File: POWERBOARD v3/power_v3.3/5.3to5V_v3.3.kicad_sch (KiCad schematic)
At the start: 22 parts, among them IC1 MAX25301AATB_V+T, IC2 MCP6541T-I_OT, IC3 AP2281-1FMG-7, J3 2053380002

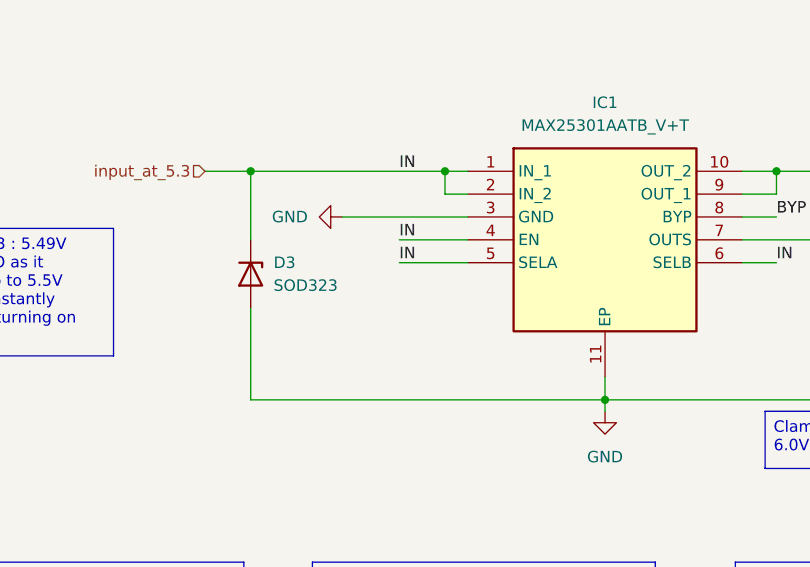
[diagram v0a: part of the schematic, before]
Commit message: Fixed D3 symbol
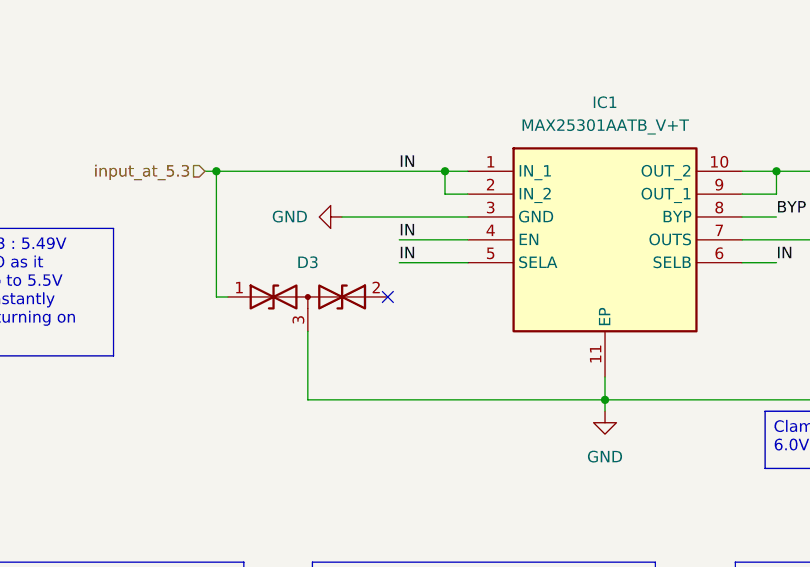
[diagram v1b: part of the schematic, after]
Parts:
- removed D3: SOD323, Package_TO_SOT_SMD:SOT-23, symbol Device:D_Zener
- added D3: SOD323, Package_TO_SOT_SMD:SOT-23, symbol Device:D_TVS_Dual_AAC
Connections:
- net GND: now also D3.3 (common)
- net input_at_5.3: now also D3.1 (A1)
- no-connect marks 2 -> 3
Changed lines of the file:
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@@
 	)
 	(junction
+		(at 95.25 57.15)
+		(diameter 0)
+		(color 0 0 0 0)
+	)
+	(junction
 		(at 205.74 57.15)
 		(diameter 0)
@@
 	)
 	(junction
-		(at 99.06 57.15)
-		(diameter 0)
-		(color 0 0 0 0)
-	)
-	(junction
 		(at 138.43 82.55)
 		(diameter 0)
@@
 	)
 	(no_connect
+		(at 114.3 71.12)
+	)
+	(no_connect
 		(at 72.39 134.62)
 	)
@@
 	(wire
 		(pts
-			(xy 228.6 116.84) (xy 240.03 116.84)
+			(xy 105.41 74.93) (xy 105.41 82.55)
 		)
 		(stroke
@@
 	(wire
 		(pts
-			(xy 153.67 67.31) (xy 157.48 67.31)
+			(xy 228.6 116.84) (xy 240.03 116.84)
 		)
 		(stroke
@@
 	(wire
 		(pts
-			(xy 62.23 168.91) (xy 62.23 175.26)
+			(xy 153.67 67.31) (xy 157.48 67.31)
 		)
 		(stroke
@@
 	(wire
 		(pts
-			(xy 231.14 82.55) (xy 236.22 82.55)
+			(xy 62.23 168.91) (xy 62.23 175.26)
 		)
 		(stroke
@@
 	(wire
 		(pts
-			(xy 99.06 72.39) (xy 99.06 82.55)
+			(xy 231.14 82.55) (xy 236.22 82.55)
 		)
 		(stroke
@@
 	(wire
 		(pts
-			(xy 99.06 82.55) (xy 138.43 82.55)
-		)
-		(stroke
-			(width 0)
-			(type default)
-		)
-	)
-	(wire
-		(pts
 			(xy 252.73 62.23) (xy 252.73 67.31)
 		)
@@
 	(wire
 		(pts
+			(xy 95.25 57.15) (xy 95.25 71.12)
+		)
+		(stroke
+			(width 0)
+			(type default)
+		)
+	)
+	(wire
+		(pts
 			(xy 179.07 152.4) (xy 189.23 152.4)
 		)
@@
 	(wire
 		(pts
+			(xy 105.41 82.55) (xy 138.43 82.55)
+		)
+		(stroke
+			(width 0)
+			(type default)
+		)
+	)
+	(wire
+		(pts
 			(xy 189.23 124.46) (xy 189.23 134.62)
 		)
@@
 	(wire
 		(pts
-			(xy 93.98 57.15) (xy 99.06 57.15)
-		)
-		(stroke
-			(width 0)
-			(type default)
-		)
-	)
-	(wire
-		(pts
 			(xy 44.45 116.84) (xy 44.45 152.4)
 		)
@@
 	(wire
 		(pts
-			(xy 99.06 57.15) (xy 99.06 64.77)
+			(xy 95.25 71.12) (xy 96.52 71.12)
 		)
 		(stroke
@@
 	(wire
 		(pts
-			(xy 99.06 57.15) (xy 120.65 57.15)
+			(xy 93.98 57.15) (xy 95.25 57.15)
 		)
 		(stroke
@@
 	(wire
 		(pts
+			(xy 95.25 57.15) (xy 120.65 57.15)
+		)
+		(stroke
+			(width 0)
+			(type default)
+		)
+	)
+	(wire
+		(pts
 			(xy 59.69 116.84) (xy 59.69 106.68)
 		)
@@
 	)
 	(symbol
-		(lib_id "Device:D_Zener")
-		(at 99.06 68.58 270)
-		(unit 1)
-		(body_style 1)
-		(exclude_from_sim no)
-		(in_bom yes)
-		(on_board yes)
-		(in_pos_files yes)
-		(dnp no)
-		(fields_autoplaced yes)
-		(property "Reference" "D3"
-			(at 101.6 67.3099 90)
-			(show_name no)
-			(do_not_autoplace no)
-			(effects
-				(font
-					(size 1.27 1.27)
-				)
-				(justify left)
-			)
-		)
-		(property "Value" "SOD323"
-			(at 101.6 69.8499 90)
-			(show_name no)
-			(do_not_autoplace no)
-			(effects
-				(font
-					(size 1.27 1.27)
-				)
-				(justify left)
-			)
-		)
-		(property "Footprint" "Package_TO_SOT_SMD:SOT-23"
-			(at 99.06 68.58 0)
-			(hide yes)
-			(show_name no)
-			(do_not_autoplace no)
-			(effects
-				(font
-					(size 1.27 1.27)
-				)
-			)
-		)
-		(property "Datasheet" "https://www.ti.com/lit/ds/symlink/esds452-q1.pdf?ts=1791562944169&ref_url=https%253A%252F%252Fwww.mouser.ch%252F"
-			(at 99.06 68.58 0)
-			(hide yes)
-			(show_name no)
-			(do_not_autoplace no)
-			(effects
-				(font
-					(size 1.27 1.27)
-				)
-			)
-		)
-		(property "Description" "Zener diode"
-			(at 99.06 68.58 0)
-			(hide yes)
-			(show_name no)
-			(do_not_autoplace no)
-			(effects
-				(font
-					(size 1.27 1.27)
-				)
-			)
-		)
-		(pin "1"
-		)
-		(pin "2"
-		)
-		(instances
-			(project "power_v3.3"
-				(path "/432bcdcf-747a-4fa0-b87b-096f44260199/9585df76-13b3-4fa5-b448-53940051778a"
-					(reference "D3")
-					(unit 1)
-				)
-			)
-		)
-	)
-	(symbol
 		(lib_id "power:GND")
 		(at 189.23 154.94 0)
@@
 					(unit 1)
 				)
+			)
+		)
+	)
+	(symbol
+		(lib_id "Device:D_TVS_Dual_AAC")
+		(at 105.41 71.12 0)
+		(unit 1)
+		(body_style 1)
+		(exclude_from_sim no)
+		(in_bom yes)
+		(on_board yes)
+		(in_pos_files yes)
+		(dnp no)
+		(fields_autoplaced yes)
+		(property "Reference" "D3"
+			(at 105.41 67.31 0)
+			(show_name no)
+			(do_not_autoplace no)
+			(effects
+				(font
+					(size 1.27 1.27)
+				)
+			)
+		)
+		(property "Value" "SOD323"
+			(at 104.1401 68.58 90)
+			(hide yes)
+			(show_name no)
+			(do_not_autoplace no)
+			(effects
+				(font
+					(size 1.27 1.27)
+				)
+				(justify left)
+			)
+		)
+		(property "Footprint" "Package_TO_SOT_SMD:SOT-23"
+			(at 101.6 71.12 0)
+			(hide yes)
+			(show_name no)
+			(do_not_autoplace no)
+			(effects
+				(font
+					(size 1.27 1.27)
+				)
+			)
+		)
+		(property "Datasheet" "https://www.ti.com/lit/ds/symlink/esds452-q1.pdf?ts=1791562944169&ref_url=https%253A%252F%252Fwww.mouser.ch%252F"
+			(at 101.6 71.12 0)
+			(hide yes)
+			(show_name no)
+			(do_not_autoplace no)
+			(effects
+				(font
+					(size 1.27 1.27)
+				)
+			)
+		)
+		(property "Description" "Bidirectional dual transient-voltage-suppression diode, center on pin 3"
+			(at 105.41 71.12 0)
+			(hide yes)
+			(show_name no)
+			(do_not_autoplace no)
+			(effects
+				(font
+					(size 1.27 1.27)
+				)
+			)
+		)
+		(pin "1"
+		)
+		(pin "3"
+		)
+		(pin "2"
+		)
+		(instances
+			(project "power_v3.3"
+				(path "/432bcdcf-747a-4fa0-b87b-096f44260199/9585df76-13b3-4fa5-b448-53940051778a"
+					(reference "D3")
+					(unit 1)
+				)

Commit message: Removed NTC from TS node
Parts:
- D3: value SOD323 -> ESDS452DBZRQ1
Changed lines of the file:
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@@
 			)
 		)
-		(property "Value" "SOD323"
+		(property "Value" "ESDS452DBZRQ1"
 			(at 104.1401 68.58 90)
 			(hide yes)

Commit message: Made BOM with Customer PNs
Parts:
- C10, C12: Added to order (none) -> Y; Customer PN (none) -> EMG-PWR-037
- C11: Added to order (none) -> Y; Customer PN (none) -> EMG-PWR-035
- C14, C15, C16, C17: Added to order (none) -> Y; Customer PN (none) -> EMG-PWR-034
- D3: Added to order (none) -> Y; Customer PN (none) -> EMG-PWR-006; Mouser Price/Stock (none) -> https://www.mouser.ch/en/ProductDetail/Texas-Instruments/ES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
- D4: Added to order (none) -> Y; Customer PN (none) -> EMG-PWR-007
- D5: Added to order (none) -> Y; Customer PN (none) -> EMG-PWR-008
- IC1: Added to order (none) -> Y; Customer PN (none) -> EMG-PWR-015
- IC2: Added to order (none) -> Y; Customer PN (none) -> EMG-PWR-016
- IC3: Added to order (none) -> Y; Customer PN (none) -> EMG-PWR-014
- J3: Added to order (none) -> Y; Customer PN (none) -> EMG-PWR-004
- LDO5V1: Added to order (none) -> NA; Customer PN (none) -> NA
- R13, R15, R17: Added to order (none) -> Y; Customer PN (none) -> EMG-PWR-022
- R14: Added to order (none) -> Y; Customer PN (none) -> EMG-PWR-021
- R16: Added to order (none) -> Y; Customer PN (none) -> EMG-PWR-020
- R18: Added to order (none) -> Y; Customer PN (none) -> EMG-PWR-019
- S2: Added to order (none) -> Y; Customer PN (none) -> EMG-PWR-012

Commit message: Added test point footprints
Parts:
- LDO5V1: Added to order NA -> (none); Customer PN NA -> EMG-PWR-042
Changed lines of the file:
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@@
 			)
 		)
-		(property "Added to order" "NA"
+		(property "Added to order" ""
 			(at 205.74 50.8 0)
 			(hide yes)
@@
 			)
 		)
-		(property "Customer PN" "NA"
+		(property "Customer PN" "EMG-PWR-042"
 			(at 205.74 50.8 0)
 			(hide yes)

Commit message: [fix]: reviewed powerboard, modified zone priority
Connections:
- net 5V_out: now reaches C17.1, IC3.5 (OUT_1), IC3.6 (OUT_2), J3.1
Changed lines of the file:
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@@
+		)
+	)
+	(label "5V_out"
+		(at 255.27 62.23 90)
+		(effects
+			(font
+				(size 1.27 1.27)
+			)
+			(justify left bottom)
 		)
 	)
